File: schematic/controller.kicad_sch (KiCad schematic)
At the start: 38 parts, among them J5 DB9_Male, J6 DB9_Male, Q4 2N3904, Q5 2N3904, U18 74LS541, U19 74LS541, U24 74LS00

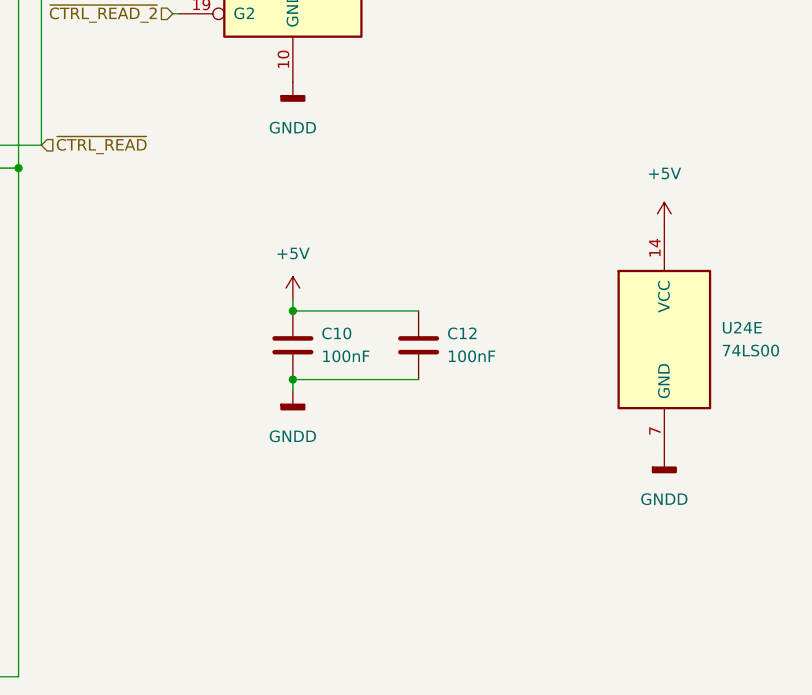
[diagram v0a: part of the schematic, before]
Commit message: adjusted size of the sheets. added pcb version to the rev field. F.0... the 0 is for future fixes on my end. RF PCB is E.0.
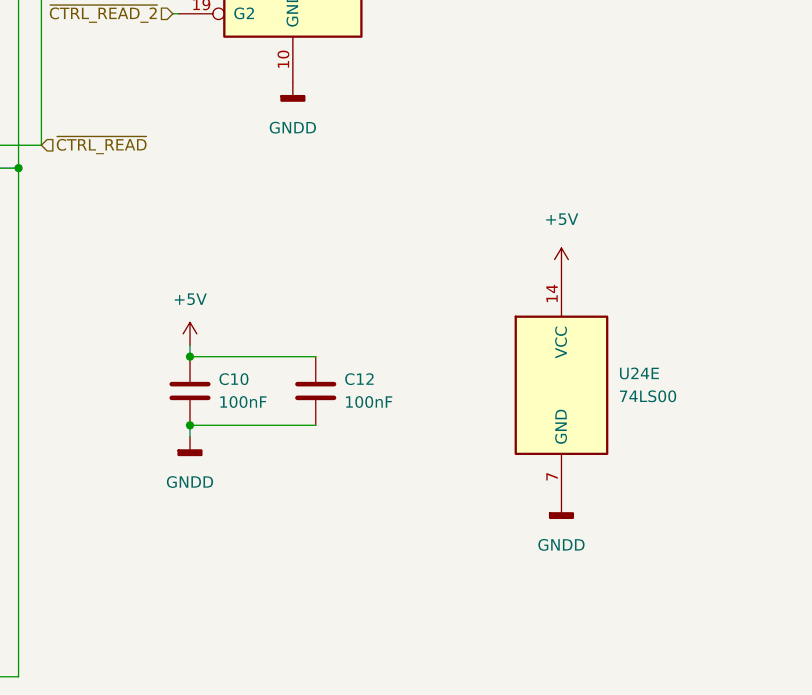
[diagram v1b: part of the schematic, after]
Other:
- title: (none) -> Colecovision Schematic
- moved on the sheet: C10, C12, U24E
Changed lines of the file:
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@@
 (kicad_sch (version 20211123) (generator eeschema)
-  (paper "A4")
+  (paper "USLetter")
+  (title_block
+    (title "Colecovision Schematic")
+    (date "2023-01-09")
+    (rev "F.0")
+    (comment 1 "Jay Convertino")
+  )
   (junction (at 240.665 27.94) (diameter 0) (color 0 0 0 0)
   )
@@
   (junction (at 43.18 139.7) (diameter 0) (color 0 0 0 0)
   )
-  (junction (at 221.615 123.19) (diameter 0) (color 0 0 0 0)
+  (junction (at 210.185 128.27) (diameter 0) (color 0 0 0 0)
   )
   (junction (at 90.805 25.4) (diameter 0) (color 0 0 0 0)
@@
   (junction (at 74.93 108.585) (diameter 0) (color 0 0 0 0)
   )
-  (junction (at 221.615 130.81) (diameter 0) (color 0 0 0 0)
+  (junction (at 210.185 135.89) (diameter 0) (color 0 0 0 0)
   )
   (junction (at 95.885 66.04) (diameter 0) (color 0 0 0 0)
@@
     (stroke (width 0) (type default) (color 0 0 0 0))
   )
-  (wire (pts (xy 221.615 121.92) (xy 221.615 123.19))
+  (wire (pts (xy 210.185 127) (xy 210.185 128.27))
     (stroke (width 0) (type default) (color 0 0 0 0))
   )
@@
     (stroke (width 0) (type default) (color 0 0 0 0))
   )
-  (wire (pts (xy 221.615 123.19) (xy 235.585 123.19))
+  (wire (pts (xy 210.185 128.27) (xy 224.155 128.27))
     (stroke (width 0) (type default) (color 0 0 0 0))
   )
@@
     (stroke (width 0) (type default) (color 0 0 0 0))
   )
-  (wire (pts (xy 221.615 132.08) (xy 221.615 130.81))
+  (wire (pts (xy 210.185 137.16) (xy 210.185 135.89))
     (stroke (width 0) (type default) (color 0 0 0 0))
   )
@@
     (stroke (width 0) (type default) (color 0 0 0 0))
   )
-  (wire (pts (xy 221.615 130.81) (xy 235.585 130.81))
+  (wire (pts (xy 210.185 135.89) (xy 224.155 135.89))
     (stroke (width 0) (type default) (color 0 0 0 0))
   )
@@
     (pin "7")
   )
-  (symbol (lib_id "Device:C") (at 221.615 127 0) (unit 1)
-    (in_bom yes) (on_board yes) (fields_autoplaced)
-    (property "Reference" "C10" (id 0) (at 224.79 125.7299 0)
-      (effects (font (size 1.27 1.27)) (justify left))
-    )
-    (property "Value" "100nF" (id 1) (at 224.79 128.2699 0)
-      (effects (font (size 1.27 1.27)) (justify left))
-    )
-    (property "Footprint" "" (id 2) (at 222.5802 130.81 0)
-      (effects (font (size 1.27 1.27)) hide)
-    )
-    (property "Datasheet" "~" (id 3) (at 221.615 127 0)
+  (symbol (lib_id "Device:C") (at 210.185 132.08 0) (unit 1)
+    (in_bom yes) (on_board yes) (fields_autoplaced)
+    (property "Reference" "C10" (id 0) (at 213.36 130.8099 0)
+      (effects (font (size 1.27 1.27)) (justify left))
+    )
+    (property "Value" "100nF" (id 1) (at 213.36 133.3499 0)
+      (effects (font (size 1.27 1.27)) (justify left))
+    )
+    (property "Footprint" "" (id 2) (at 211.1502 135.89 0)
+      (effects (font (size 1.27 1.27)) hide)
+    )
+    (property "Datasheet" "~" (id 3) (at 210.185 132.08 0)
       (effects (font (size 1.27 1.27)) hide)
     )
@@
     (pin "1")
   )
-  (symbol (lib_id "power:+5V") (at 221.615 121.92 0) (unit 1)
-    (in_bom yes) (on_board yes) (fields_autoplaced)
-    (property "Reference" "#PWR?" (id 0) (at 221.615 125.73 0)
-      (effects (font (size 1.27 1.27)) hide)
-    )
-    (property "Value" "+5V" (id 1) (at 221.615 116.84 0))
-    (property "Footprint" "" (id 2) (at 221.615 121.92 0)
-      (effects (font (size 1.27 1.27)) hide)
-    )
-    (property "Datasheet" "" (id 3) (at 221.615 121.92 0)
-      (effects (font (size 1.27 1.27)) hide)
-    )
-    (pin "1")
-  )
-  (symbol (lib_id "power:GNDD") (at 262.89 139.065 0) (unit 1)
-    (in_bom yes) (on_board yes) (fields_autoplaced)
-    (property "Reference" "#PWR?" (id 0) (at 262.89 145.415 0)
-      (effects (font (size 1.27 1.27)) hide)
-    )
-    (property "Value" "GNDD" (id 1) (at 262.89 144.145 0))
-    (property "Footprint" "" (id 2) (at 262.89 139.065 0)
-      (effects (font (size 1.27 1.27)) hide)
-    )
-    (property "Datasheet" "" (id 3) (at 262.89 139.065 0)
+  (symbol (lib_id "power:+5V") (at 210.185 127 0) (unit 1)
+    (in_bom yes) (on_board yes) (fields_autoplaced)
+    (property "Reference" "#PWR?" (id 0) (at 210.185 130.81 0)
+      (effects (font (size 1.27 1.27)) hide)
+    )
+    (property "Value" "+5V" (id 1) (at 210.185 121.92 0))
+    (property "Footprint" "" (id 2) (at 210.185 127 0)
+      (effects (font (size 1.27 1.27)) hide)
+    )
+    (property "Datasheet" "" (id 3) (at 210.185 127 0)
+      (effects (font (size 1.27 1.27)) hide)
+    )
+    (pin "1")
+  )
+  (symbol (lib_id "power:GNDD") (at 251.46 144.145 0) (unit 1)
+    (in_bom yes) (on_board yes) (fields_autoplaced)
+    (property "Reference" "#PWR?" (id 0) (at 251.46 150.495 0)
+      (effects (font (size 1.27 1.27)) hide)
+    )
+    (property "Value" "GNDD" (id 1) (at 251.46 149.225 0))
+    (property "Footprint" "" (id 2) (at 251.46 144.145 0)
+      (effects (font (size 1.27 1.27)) hide)
+    )
+    (property "Datasheet" "" (id 3) (at 251.46 144.145 0)
       (effects (font (size 1.27 1.27)) hide)
     )
@@
     (pin "1")
   )
-  (symbol (lib_id "Device:C") (at 235.585 127 0) (unit 1)
-    (in_bom yes) (on_board yes) (fields_autoplaced)
-    (property "Reference" "C12" (id 0) (at 238.76 125.7299 0)
-      (effects (font (size 1.27 1.27)) (justify left))
-    )
-    (property "Value" "100nF" (id 1) (at 238.76 128.2699 0)
-      (effects (font (size 1.27 1.27)) (justify left))
-    )
-    (property "Footprint" "" (id 2) (at 236.5502 130.81 0)
-      (effects (font (size 1.27 1.27)) hide)
-    )
-    (property "Datasheet" "~" (id 3) (at 235.585 127 0)
+  (symbol (lib_id "Device:C") (at 224.155 132.08 0) (unit 1)
+    (in_bom yes) (on_board yes) (fields_autoplaced)
+    (property "Reference" "C12" (id 0) (at 227.33 130.8099 0)
+      (effects (font (size 1.27 1.27)) (justify left))
+    )
+    (property "Value" "100nF" (id 1) (at 227.33 133.3499 0)
+      (effects (font (size 1.27 1.27)) (justify left))
+    )
+    (property "Footprint" "" (id 2) (at 225.1202 135.89 0)
+      (effects (font (size 1.27 1.27)) hide)
+    )
+    (property "Datasheet" "~" (id 3) (at 224.155 132.08 0)
       (effects (font (size 1.27 1.27)) hide)
     )
@@
     (pin "1")
   )
-  (symbol (lib_id "74xx:74LS00") (at 262.89 126.365 0) (unit 5)
-    (in_bom yes) (on_board yes) (fields_autoplaced)
-    (property "Reference" "U24" (id 0) (at 269.24 125.0949 0)
-      (effects (font (size 1.27 1.27)) (justify left))
-    )
-    (property "Value" "74LS00" (id 1) (at 269.24 127.6349 0)
-      (effects (font (size 1.27 1.27)) (justify left))
-    )
-    (property "Footprint" "" (id 2) (at 262.89 126.365 0)
-      (effects (font (size 1.27 1.27)) hide)
-    )
-    (property "Datasheet" "http://www.ti.com/lit/gpn/sn74ls00" (id 3) (at 262.89 126.365 0)
+  (symbol (lib_id "74xx:74LS00") (at 251.46 131.445 0) (unit 5)
+    (in_bom yes) (on_board yes) (fields_autoplaced)
+    (property "Reference" "U24" (id 0) (at 257.81 130.1749 0)
+      (effects (font (size 1.27 1.27)) (justify left))
+    )
+    (property "Value" "74LS00" (id 1) (at 257.81 132.7149 0)
+      (effects (font (size 1.27 1.27)) (justify left))
+    )
+    (property "Footprint" "" (id 2) (at 251.46 131.445 0)
+      (effects (font (size 1.27 1.27)) hide)
+    )
+    (property "Datasheet" "http://www.ti.com/lit/gpn/sn74ls00" (id 3) (at 251.46 131.445 0)
       (effects (font (size 1.27 1.27)) hide)
     )
@@
     (pin "9")
   )
-  (symbol (lib_id "power:+5V") (at 262.89 113.665 0) (unit 1)
-    (in_bom yes) (on_board yes) (fields_autoplaced)
-    (property "Reference" "#PWR?" (id 0) (at 262.89 117.475 0)
-      (effects (font (size 1.27 1.27)) hide)
-    )
-    (property "Value" "+5V" (id 1) (at 262.89 107.95 0))
-    (property "Footprint" "" (id 2) (at 262.89 113.665 0)
-      (effects (font (size 1.27 1.27)) hide)
-    )
-    (property "Datasheet" "" (id 3) (at 262.89 113.665 0)
+  (symbol (lib_id "power:+5V") (at 251.46 118.745 0) (unit 1)
+    (in_bom yes) (on_board yes) (fields_autoplaced)
+    (property "Reference" "#PWR?" (id 0) (at 251.46 122.555 0)
+      (effects (font (size 1.27 1.27)) hide)
+    )
+    (property "Value" "+5V" (id 1) (at 251.46 113.03 0))
+    (property "Footprint" "" (id 2) (at 251.46 118.745 0)
+      (effects (font (size 1.27 1.27)) hide)
+    )
+    (property "Datasheet" "" (id 3) (at 251.46 118.745 0)
       (effects (font (size 1.27 1.27)) hide)
     )
@@
     (pin "1")
   )
-  (symbol (lib_id "power:GNDD") (at 221.615 132.08 0) (unit 1)
-    (in_bom yes) (on_board yes) (fields_autoplaced)
-    (property "Reference" "#PWR?" (id 0) (at 221.615 138.43 0)
-      (effects (font (size 1.27 1.27)) hide)
-    )
-    (property "Value" "GNDD" (id 1) (at 221.615 137.16 0))
-    (property "Footprint" "" (id 2) (at 221.615 132.08 0)
-      (effects (font (size 1.27 1.27)) hide)
-    )
-    (property "Datasheet" "" (id 3) (at 221.615 132.08 0)
-      (effects (font (size 1.27 1.27)) hide)
-    )
+  (symbol (lib_id "power:GNDD") (at 210.185 137.16 0) (unit 1)
+    (in_bom yes) (on_board yes) (fields_autoplaced)
+    (property "Reference" "#PWR?" (id 0) (at 210.185 143.51 0)
+      (effects (font (size 1.27 1.27)) hide)
+    )
+    (property "Value" "GNDD" (id 1) (at 210.185 142.24 0))
+    (property "Footprint" "" (id 2) (at 210.185 137.16 0)
+      (effects (font (size 1.27 1.27)) hide)
+    )
+    (property "Datasheet" "" (id 3) (at 210.185 137.16 0)
+      (effects (font (size 1.27 1.27)) hide)
+    )

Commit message: cleanup, and started associating components
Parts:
- C10, C101, C103, C12, C17, C19, C61, C65, C98, C99: footprint (none) -> Capacitor_THT:C_Disc_D10.0mm_W2.5mm_P5.00mm
- C102, C104: footprint (none) -> Capacitor_THT:C_Disc_D7.0mm_W2.5mm_P5.00mm
- CR1, CR2: footprint (none) -> Diode_THT:D_DO-35_SOD27_P7.62mm_Horizontal
- J5, J6: footprint (none) -> Connector_Dsub:DSUB-9_Male_Horizontal_P2.77x2.54mm_EdgePinOffset9.40mm
- Q4, Q5: footprint Package_TO_SOT_THT:TO-92_Inline -> Package_TO_SOT_THT:TO-92_Wide
- R1, R19, R20, R21, R22, R23, R24, R25, R27, R65, R67, R69, R70, R71, R72: footprint (none) -> Resistor_THT:R_Axial_DIN0207_L6.3mm_D2.5mm_P7.62mm_Horizontal
- U18, U19: footprint (none) -> Package_DIP:DIP-20_W7.62mm_LongPads
- U24: footprint (none) -> Package_DIP:DIP-14_W7.62mm_LongPads

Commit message: first draft of board with components added, no traces
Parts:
- C10, C101, C103, C12, C17, C19, C61, C65, C98, C99: footprint Capacitor_THT:C_Disc_D10.0mm_W2.5mm_P5.00mm -> Capacitor_THT:C_Disc_D7.0mm_W2.5mm_P5.00mm
- CR1, CR2: footprint Diode_THT:D_DO-35_SOD27_P7.62mm_Horizontal -> Diode_THT:D_DO-35_SOD27_P10.16mm_Horizontal
- R1, R19, R20, R21, R22, R23, R24, R25, R27, R65, R67, R69, R70, R71, R72: footprint Resistor_THT:R_Axial_DIN0207_L6.3mm_D2.5mm_P7.62mm_Horizontal -> Resistor_THT:R_Axial_DIN0207_L6.3mm_D2.5mm_P10.16mm_Horizontal

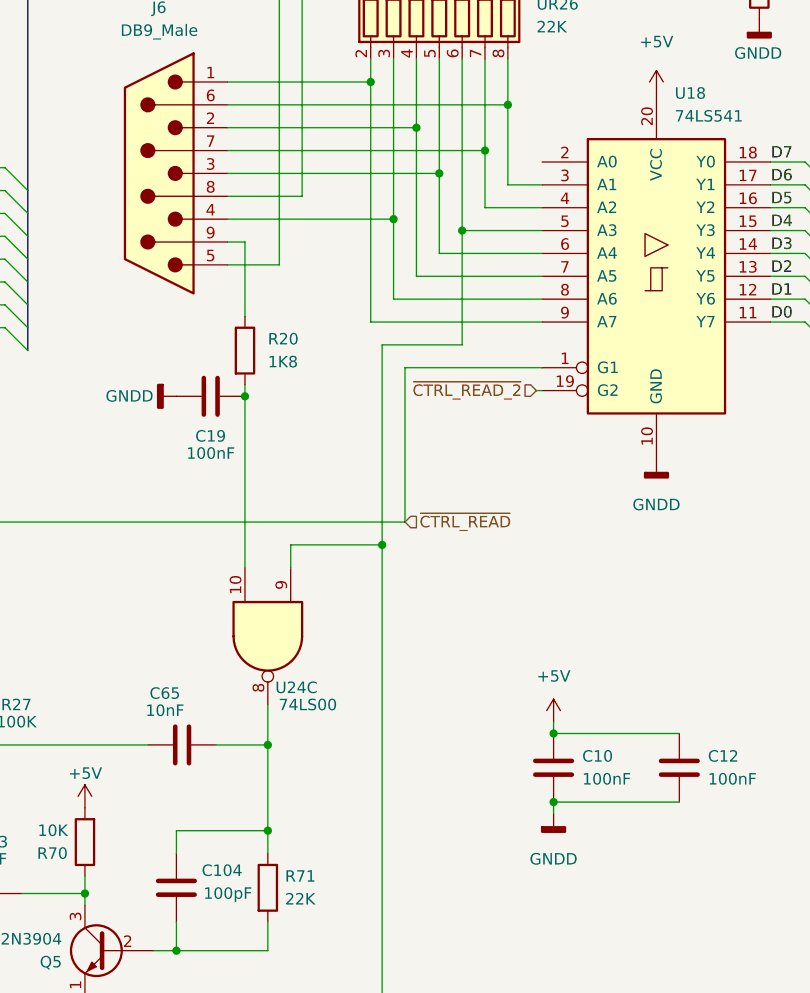
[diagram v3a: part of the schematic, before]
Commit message: added controller traces and some around it.
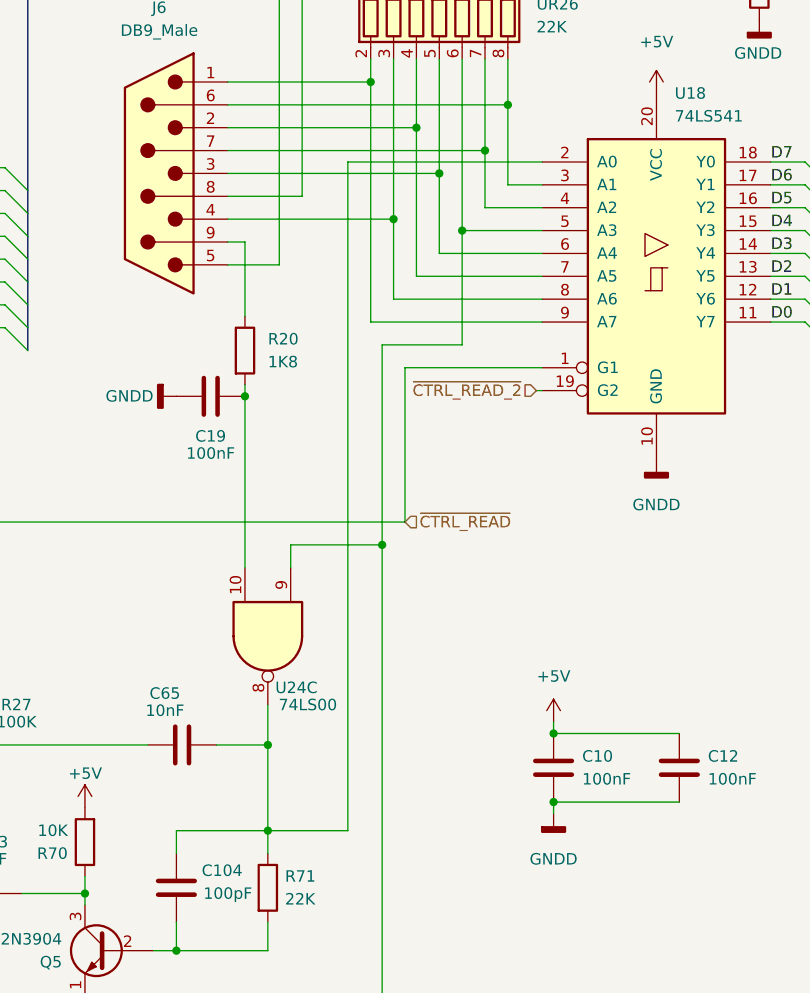
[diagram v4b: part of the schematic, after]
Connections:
- net at U18.2 (A0): now also C104.2, C65.2, R71.1, U24.8
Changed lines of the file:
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@@
+    (stroke (width 0) (type default) (color 0 0 0 0))
+  )
+  (wire (pts (xy 208.915 64.77) (xy 187.325 64.77))
     (stroke (width 0) (type default) (color 0 0 0 0))
   )
@@
     (stroke (width 0) (type default) (color 0 0 0 0))
   )
+  (wire (pts (xy 187.325 64.77) (xy 187.325 139.065))
+    (stroke (width 0) (type default) (color 0 0 0 0))
+  )
   (wire (pts (xy 180.975 109.855) (xy 180.975 107.315))
     (stroke (width 0) (type default) (color 0 0 0 0))
@@
     (stroke (width 0) (type default) (color 0 0 0 0))
   )
+  (wire (pts (xy 187.325 139.065) (xy 178.435 139.065))
+    (stroke (width 0) (type default) (color 0 0 0 0))
+  )

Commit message: added new models, fixed the drc errors. changed power width.
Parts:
- J5, J6: footprint Connector_Dsub:DSUB-9_Male_Horizontal_P2.77x2.54mm_EdgePinOffset9.40mm -> Connector_Dsub:DSUB-9_Male_Horizontal_P2.77x2.84mm_EdgePinOffset7.70mm_Housed_MountingHolesOffset9.12mm
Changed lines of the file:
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@@
     (property "Reference" "J6" (id 0) (at 166.37 47.625 0))
     (property "Value" "DB9_Male" (id 1) (at 166.37 50.165 0))
-    (property "Footprint" "Connector_Dsub:DSUB-9_Male_Horizontal_P2.77x2.54mm_EdgePinOffset9.40mm" (id 2) (at 166.37 66.04 0)
+    (property "Footprint" "Connector_Dsub:DSUB-9_Male_Horizontal_P2.77x2.84mm_EdgePinOffset7.70mm_Housed_MountingHolesOffset9.12mm" (id 2) (at 166.37 66.04 0)
       (effects (font (size 1.27 1.27)) hide)
     )
@@
     (property "Reference" "J5" (id 0) (at 50.165 50.165 0))
     (property "Value" "DB9_Male" (id 1) (at 50.165 52.705 0))
-    (property "Footprint" "Connector_Dsub:DSUB-9_Male_Horizontal_P2.77x2.54mm_EdgePinOffset9.40mm" (id 2) (at 50.165 68.58 0)
-      (effects (font (size 1.27 1.27)) hide)
-    )
+    (property "Footprint" "Connector_Dsub:DSUB-9_Male_Horizontal_P2.77x2.84mm_EdgePinOffset7.70mm_Housed_MountingHolesOffset9.12mm" (id 2) (at 50.165 68.58 0)
+      (effects (font (size 1.27 1.27)) hide)
+    )

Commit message: updated schematic with new layout
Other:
- company: (none) -> sparkletron
- title: Colecovision Schematic -> Reverse Engineer Colecovision
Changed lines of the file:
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@@
   (paper "USLetter")
   (title_block
-    (title "Colecovision Schematic")
-    (date "2023-01-09")
-    (rev "F.0")
+    (title "Reverse Engineer Colecovision")
+    (date "2023-03-14")
+    (rev "DEV")
+    (company "sparkletron")
     (comment 1 "Jay Convertino")
+    (comment 2 "MIT LICENSE")
   )
   (junction (at 240.665 27.94) (diameter 0) (color 0 0 0 0)
